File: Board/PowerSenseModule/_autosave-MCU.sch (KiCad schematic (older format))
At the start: 37 parts, among them J3 Programming Header, J4 Conn_01x02_Male, U2 NCV2007x, U3 dsPIC33EV32GM102, U4 MCP2542FDxMF, Y1 Crystal

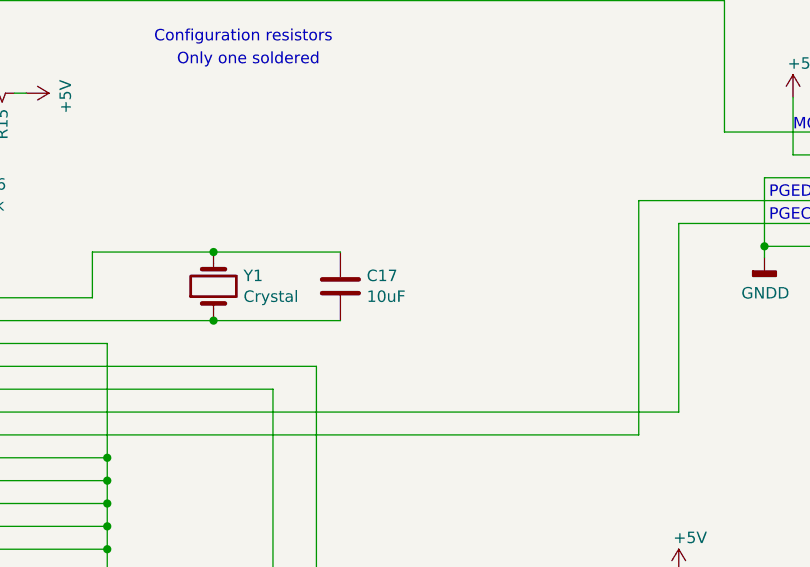
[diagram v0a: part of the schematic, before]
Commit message: Every component wired.
Each component is wired. I've now decided to make this PCB symmetric though.
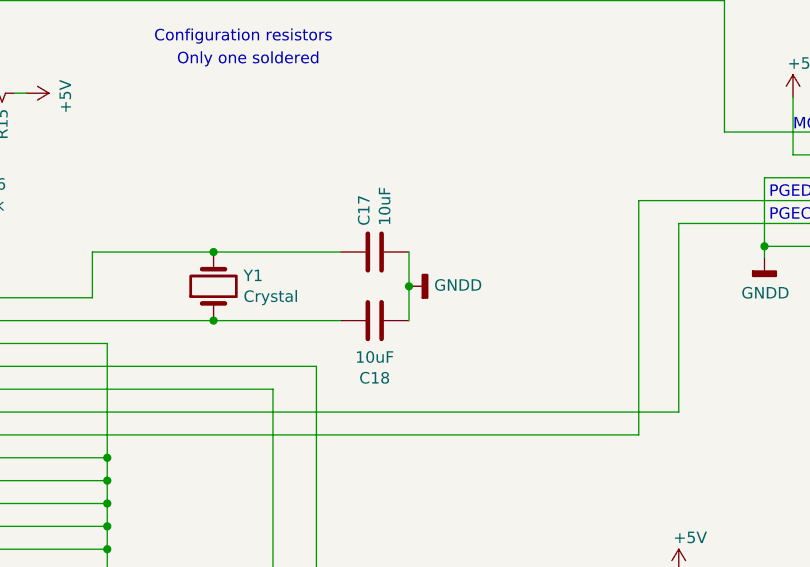
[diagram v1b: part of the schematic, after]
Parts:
- added C18: 10uF, Capacitor_SMD:C_0603_1608Metric_Pad1.05x0.95mm_HandSolder, symbol Device:C
- Y1: footprint Crystal:Crystal_SMD_2520-4Pin_2.5x2.0mm -> Crystal_SMD_2520-4Pin_2.5x2.0mm.kicad_mod_IEEE.kicad_mod
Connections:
- net GNDD: now also C17.2, C18.2
- net at U3.10 (OSC2/CLKO/RPI19/RA3), Y1.1: now also C18.1; no longer C17.2
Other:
- moved on the sheet: C17
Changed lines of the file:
@@
 F 0 "Y1" V 6686 1919 50  0000 R CNN
 F 1 "Crystal" V 6595 1919 50  0000 R CNN
-F 2 "Crystal:Crystal_SMD_2520-4Pin_2.5x2.0mm" H 6640 2050 50  0001 C CNN
+F 2 "Crystal_SMD_2520-4Pin_2.5x2.0mm.kicad_mod_IEEE.kicad_mod" H 6640 2050 50  0001 C CNN
 F 3 "https://www.mouser.com/datasheet/2/3/ABM10AIG-783578.pdf" H 6640 2050 50  0001 C CNN
 	1    6640 2050
@@
 L Device:C C17
 U 1 1 5D7A1F19
-P 7195 2050
-F 0 "C17" H 7310 2096 50  0000 L CNN
-F 1 "10uF" H 7310 2005 50  0000 L CNN
-F 2 "Capacitor_SMD:C_0603_1608Metric_Pad1.05x0.95mm_HandSolder" H 7233 1900 50  0001 C CNN
-F 3 "~" H 7195 2050 50  0001 C CNN
-	1    7195 2050
-	1    0    0    -1
+P 7345 1900
+F 0 "C17" H 7460 1946 50  0000 L CNN
+F 1 "10uF" H 7460 1855 50  0000 L CNN
+F 2 "Capacitor_SMD:C_0603_1608Metric_Pad1.05x0.95mm_HandSolder" H 7383 1750 50  0001 C CNN
+F 3 "~" H 7345 1900 50  0001 C CNN
+	1    7345 1900
+	0    -1   -1   0
 $EndComp
 Wire Wire Line
 	6640 2200 7195 2200
+$Comp
+L Device:C C18
+U 1 1 5D95386F
+P 7345 2200
+F 0 "C18" V 7093 2200 50  0000 C CNN
+F 1 "10uF" V 7184 2200 50  0000 C CNN
+F 2 "Capacitor_SMD:C_0603_1608Metric_Pad1.05x0.95mm_HandSolder" H 7383 2050 50  0001 C CNN
+F 3 "~" H 7345 2200 50  0001 C CNN
+	1    7345 2200
+	0    -1   -1   0
+$EndComp
 Wire Wire Line
 	6640 1900 7195 1900
+Wire Wire Line
+	7495 1900 7495 2050
+$Comp
+L power:GNDD #PWR?
+U 1 1 5D766394
+P 7495 2050
+F 0 "#PWR?" H 7495 1800 50  0001 C CNN
+F 1 "GNDD" V 7499 1940 50  0000 R CNN
+F 2 "" H 7495 2050 50  0001 C CNN
+F 3 "" H 7495 2050 50  0001 C CNN
+	1    7495 2050
+	0    -1   -1   0
+$EndComp
+Connection ~ 7495 2050
+Wire Wire Line
+	7495 2050 7495 2200
 $EndSCHEMATC
